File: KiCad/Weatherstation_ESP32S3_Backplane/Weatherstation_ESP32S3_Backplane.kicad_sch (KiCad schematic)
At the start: 50 parts, among them J1 01x02 JST XH, J10 01x04 Molex KK254, J11 01x02 JST XH, J12 01x04 Molex KK254, J13 01x22 Generic socket, J14 01x22 Generic socket, J15 01x04 Generic header, J16 01x02 JST XH, J17 01x04 Molex KK254, J18 01x02 JST XH, J19 01x06 Generic socket, J2 01x03 JST XH, J20 01x06 Generic socket, J3 01x03 JST XH, J4 01x07 Generic socket, J5 01x08 Generic socket, J6 01x08 Generic socket, J7 01x04 JST XH, J8 01x04 Molex KK254, J9 282834-2 Screw Terminal, Q1 RFP12N10L, U1 LM7805, U2 MAX6675ISA+T

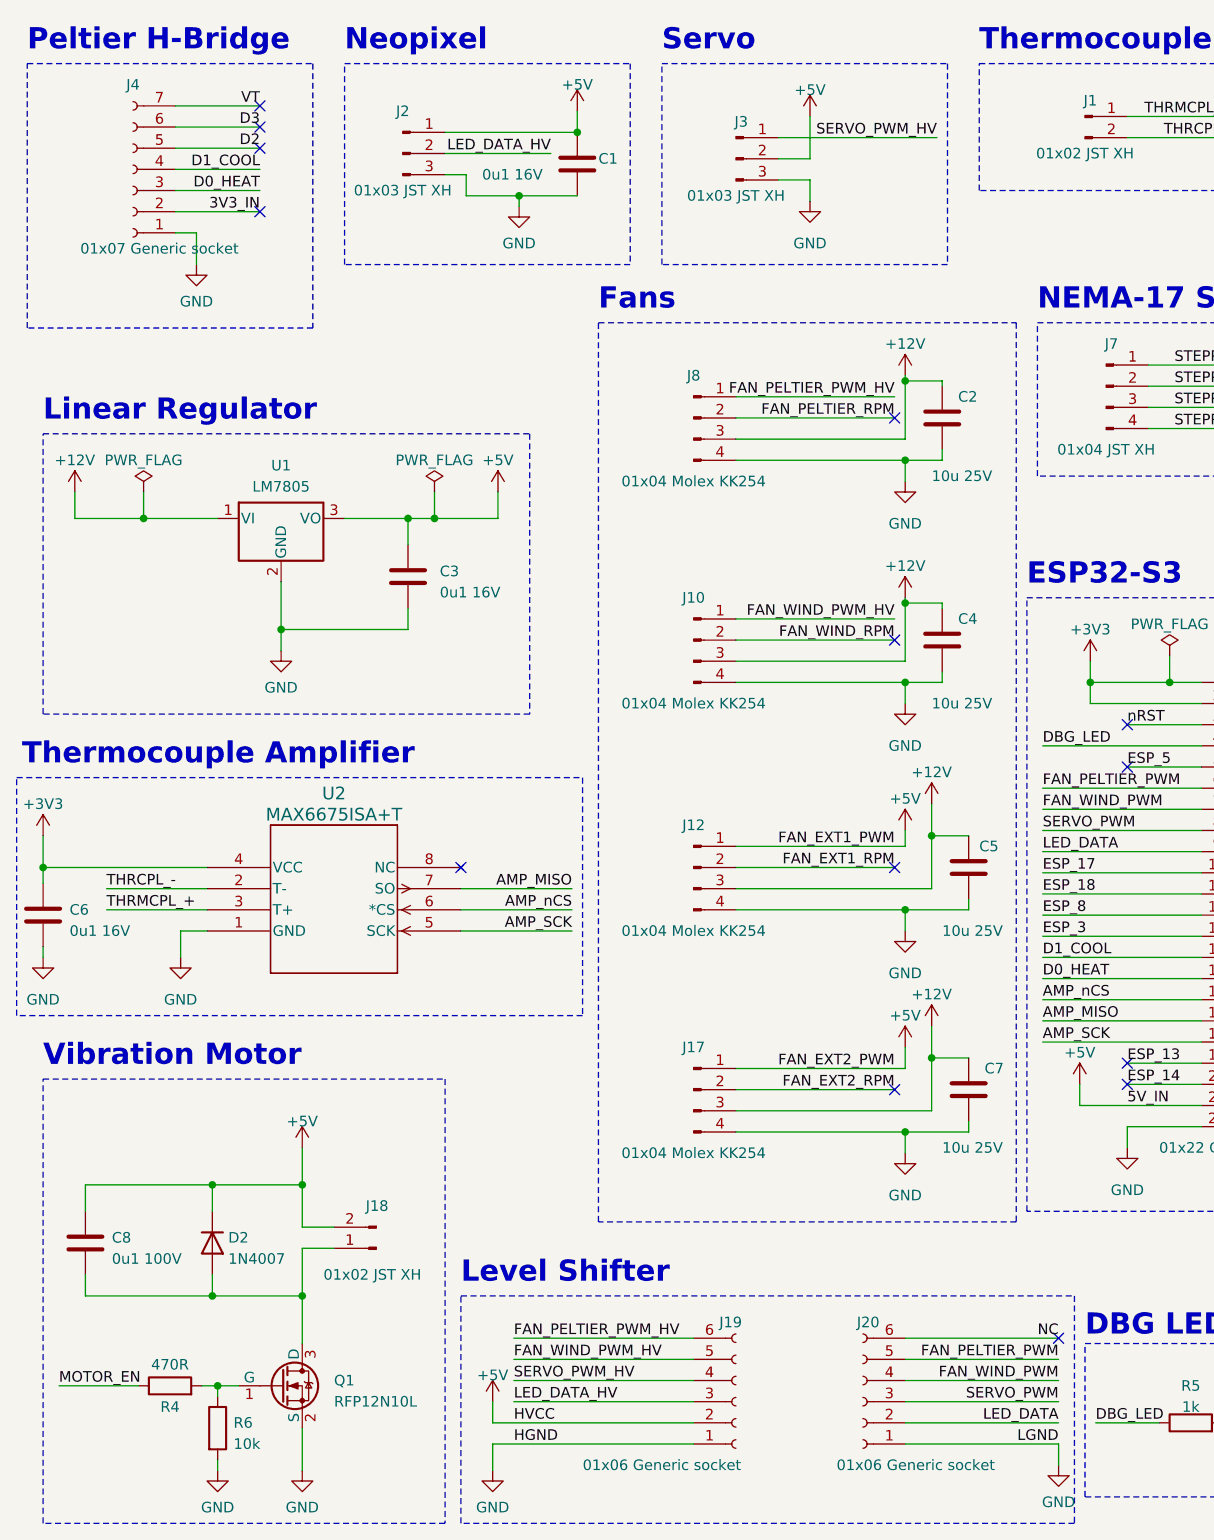
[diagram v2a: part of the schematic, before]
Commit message: Fixed known issues with PCB: Connected neopixel directly to ESP32, not through level shifter; Exchanged drain & source of vibration motor MOSFET; Added 0,33uF MLCC between pin 1 and gnd of LM7805;
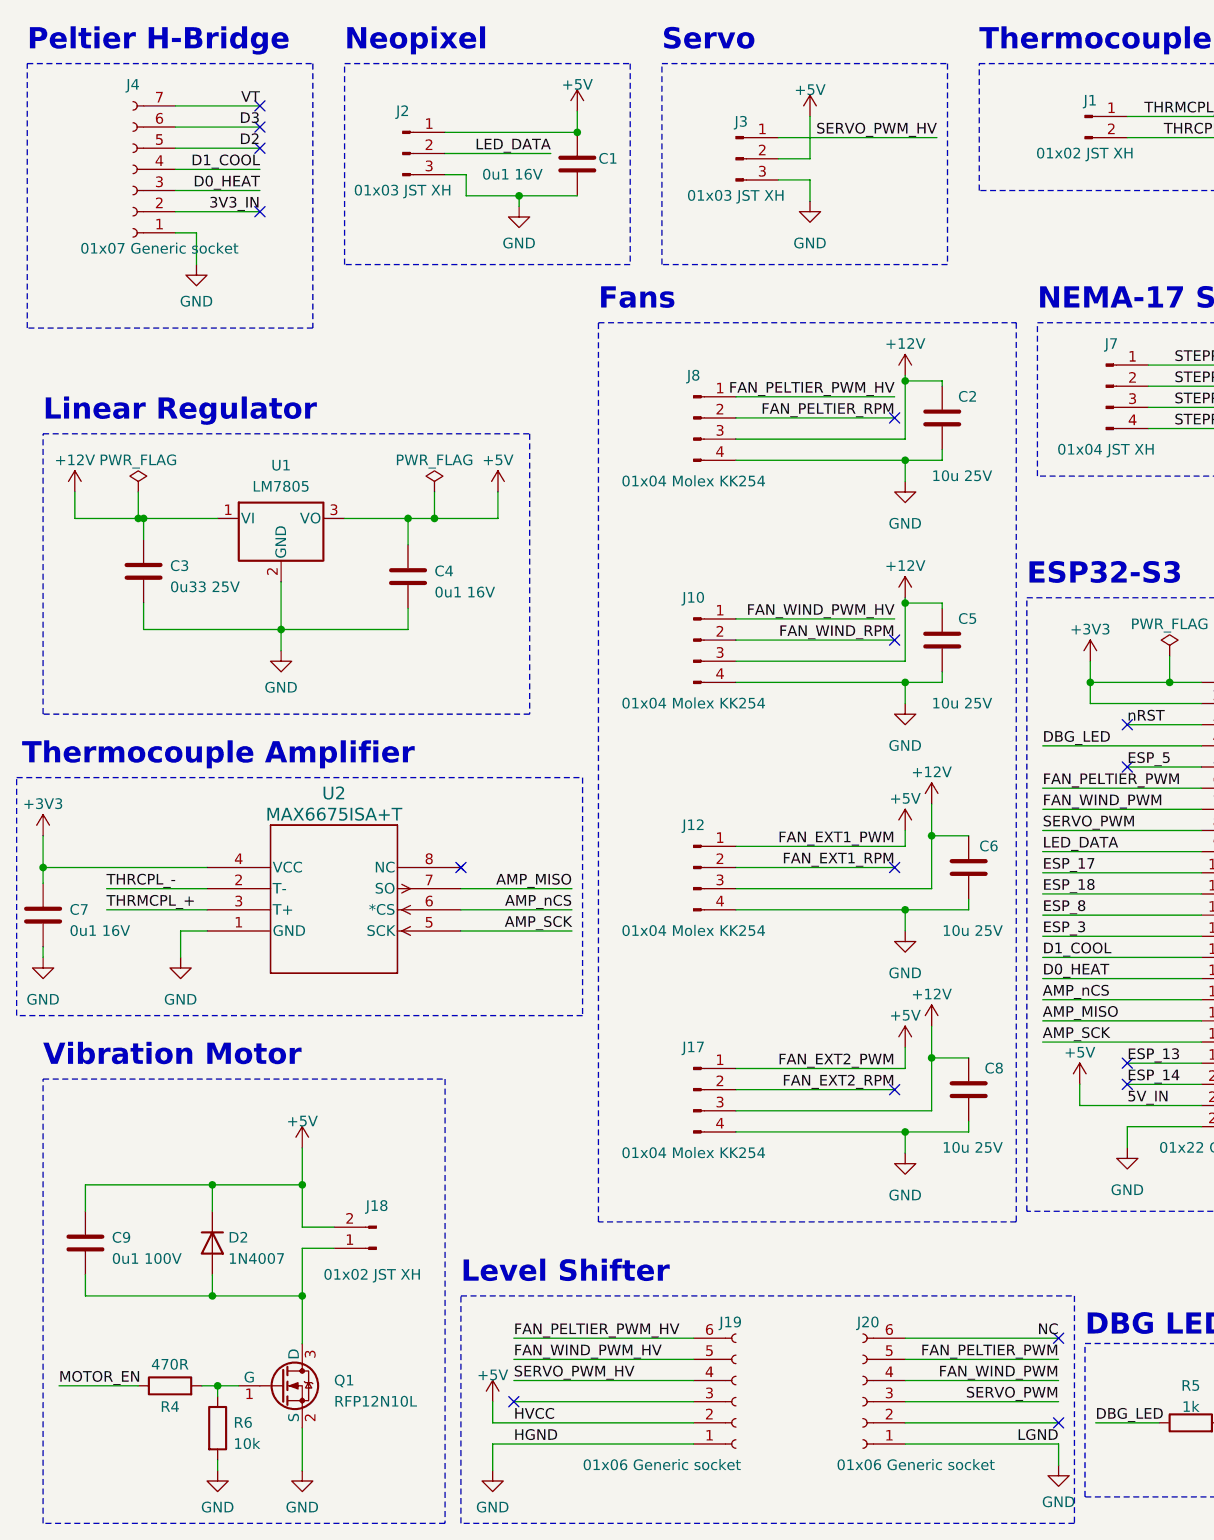
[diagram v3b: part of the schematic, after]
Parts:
- added C3: 0u33 25V, Capacitor_SMD:C_1206_3216Metric, symbol Device:C
- renumbered C3 to C4, C4 to C5, C5 to C6, C6 to C7, C7 to C8, C8 to C9
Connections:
- net +12V: now also C3.1
- net GND: now also C3.2
- net LED_DATA: now also J2.2 (Pin_2); no longer J20.2 (Pin_2)
- net LED_DATA_HV: no longer names the net of J19.3 (Pin_3)
- net LED_DATA_HV: no longer J2.2 (Pin_2)
- no-connect marks 29 -> 31
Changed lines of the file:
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@@
   (junction (at 120.65 147.32) (diameter 0) (color 0 0 0 0)
   )
+  (junction (at 28.575 73.66) (diameter 0) (color 0 0 0 0)
+  )
   (junction (at 120.65 120.65) (diameter 0) (color 0 0 0 0)
   )
@@
   )
   (no_connect (at 119.38 61.595))
+  (no_connect (at 139.065 182.245))
   (no_connect (at 203.2 95.885))
   (no_connect (at 119.38 88.265))
@@
   (no_connect (at 203.2 139.065))
   (no_connect (at 203.2 103.505))
+  (no_connect (at 73.66 179.705))
   (no_connect (at 43.18 36.83))
   (no_connect (at 43.18 29.21))
@@
     (stroke (width 0) (type default))
   )
-  (wire (pts (xy 20.955 73.66) (xy 29.21 73.66))
+  (wire (pts (xy 28.575 73.66) (xy 29.21 73.66))
+    (stroke (width 0) (type default))
+  )
+  (wire (pts (xy 20.955 73.66) (xy 28.575 73.66))
     (stroke (width 0) (type default))
   )
@@
     (stroke (width 0) (type default))
   )
+  (wire (pts (xy 45.72 86.995) (xy 29.21 86.995))
+    (stroke (width 0) (type default))
+  )
   (wire (pts (xy 123.825 111.76) (xy 128.27 111.76))
     (stroke (width 0) (type default))
@@
     (stroke (width 0) (type default))
   )
-  (wire (pts (xy 29.21 70.485) (xy 29.21 73.66))
-    (stroke (width 0) (type default))
-  )
   (wire (pts (xy 125.095 66.675) (xy 125.095 65.405))
     (stroke (width 0) (type default))
@@
     (stroke (width 0) (type default))
   )
+  (wire (pts (xy 29.21 73.66) (xy 29.21 76.2))
+    (stroke (width 0) (type default))
+  )
   (wire (pts (xy 128.27 147.32) (xy 128.27 146.05))
     (stroke (width 0) (type default))
@@
     (stroke (width 0) (type default))
   )
+  (wire (pts (xy 29.21 86.995) (xy 29.21 83.82))
+    (stroke (width 0) (type default))
+  )
   (wire (pts (xy 80.645 120.65) (xy 67.31 120.65))
     (stroke (width 0) (type default))
@@
     (stroke (width 0) (type default))
   )
+  (wire (pts (xy 28.575 70.485) (xy 28.575 73.66))
+    (stroke (width 0) (type default))
+  )
   (wire (pts (xy 120.65 147.32) (xy 120.65 149.86))
     (stroke (width 0) (type default))
@@
     (effects (font (size 1.27 1.27)) (justify right bottom))
   )
-  (label "LED_DATA_HV" (at 78.105 29.845 180) (fields_autoplaced)
+  (label "LED_DATA" (at 78.105 29.845 180) (fields_autoplaced)
     (effects (font (size 1.27 1.27)) (justify right bottom))
   )
@@
     (effects (font (size 1.27 1.27)) (justify right bottom))
   )
-  (label "LED_DATA" (at 139.065 182.245 180) (fields_autoplaced)
-    (effects (font (size 1.27 1.27)) (justify right bottom))
-  )
   (label "STEPPER_VM" (at 271.78 29.845 180) (fields_autoplaced)
     (effects (font (size 1.27 1.27)) (justify right bottom))
@@
     (effects (font (size 1.27 1.27)) (justify left bottom))
   )
-  (label "LED_DATA_HV" (at 73.66 179.705 0) (fields_autoplaced)
-    (effects (font (size 1.27 1.27)) (justify left bottom))
-  )
   (label "STEPPER_DIR" (at 213.36 47.625 0) (fields_autoplaced)
     (effects (font (size 1.27 1.27)) (justify left bottom))
@@
   (symbol (lib_id "Device:C") (at 128.27 115.57 0) (unit 1)
     (in_bom yes) (on_board yes) (dnp no)
-    (property "Reference" "C5" (at 129.54 113.03 0)
+    (property "Reference" "C6" (at 129.54 113.03 0)
       (effects (font (size 1.27 1.27)) (justify left))
     )
@@
       (project "Weatherstation_ESP32S3_Backplane"
         (path "/9f32fcd7-b7a2-400b-a555-9213e4bd23ed"
-          (reference "C5") (unit 1)
+          (reference "C6") (unit 1)
         )
       )
@@
     )
   )
+  (symbol (lib_id "Device:C") (at 29.21 80.01 0) (unit 1)
+    (in_bom yes) (on_board yes) (dnp no)
+    (property "Reference" "C3" (at 32.385 79.375 0)
+      (effects (font (size 1.27 1.27)) (justify left))
+    )
+    (property "Value" "0u33 25V" (at 32.385 81.915 0)
+      (effects (font (size 1.27 1.27)) (justify left))
+    )
+    (property "Footprint" "Capacitor_SMD:C_1206_3216Metric" (at 30.1752 83.82 0)
+      (effects (font (size 1.27 1.27)) hide)
+    )
+    (property "Datasheet" "~" (at 29.21 80.01 0)
+      (effects (font (size 1.27 1.27)) hide)
+    )
+    (property "LCSC Part #" "C1525" (at 29.21 80.01 0)
+      (effects (font (size 1.27 1.27)) hide)
+    )
+    (pin "1")
+    (pin "2")
+    (instances
+      (project "Weatherstation_ESP32S3_Backplane"
+        (path "/9f32fcd7-b7a2-400b-a555-9213e4bd23ed"
+          (reference "C3") (unit 1)
+        )
+      )
+    )
+  )
   (symbol (lib_id "Mechanical:MountingHole") (at 264.16 109.22 0) (unit 1)
     (in_bom yes) (on_board yes) (dnp no) (fields_autoplaced)
@@
   )
   (symbol (lib_id "Device:C") (at 60.96 80.645 0) (unit 1)
-    (in_bom yes) (on_board yes) (dnp no) (fields_autoplaced)
-    (property "Reference" "C3" (at 64.77 80.01 0)
+    (in_bom yes) (on_board yes) (dnp no)
+    (property "Reference" "C4" (at 64.135 80.01 0)
       (effects (font (size 1.27 1.27)) (justify left))
     )
-    (property "Value" "0u1 16V" (at 64.77 82.55 0)
+    (property "Value" "0u1 16V" (at 64.135 82.55 0)
       (effects (font (size 1.27 1.27)) (justify left))
     )
@@
       (project "Weatherstation_ESP32S3_Backplane"
         (path "/9f32fcd7-b7a2-400b-a555-9213e4bd23ed"
-          (reference "C3") (unit 1)
+          (reference "C4") (unit 1)
         )
       )
@@
   (symbol (lib_id "Device:C") (at 125.095 88.265 0) (unit 1)
     (in_bom yes) (on_board yes) (dnp no)
-    (property "Reference" "C4" (at 127 85.725 0)
+    (property "Reference" "C5" (at 127 85.725 0)
       (effects (font (size 1.27 1.27)) (justify left))
     )
@@
       (project "Weatherstation_ESP32S3_Backplane"
         (path "/9f32fcd7-b7a2-400b-a555-9213e4bd23ed"
-          (reference "C4") (unit 1)
+          (reference "C5") (unit 1)
         )
       )
@@
   (symbol (lib_id "Device:C") (at 17.145 121.285 180) (unit 1)
     (in_bom yes) (on_board yes) (dnp no) (fields_autoplaced)
-    (property "Reference" "C6" (at 20.32 120.65 0)
+    (property "Reference" "C7" (at 20.32 120.65 0)
       (effects (font (size 1.27 1.27)) (justify right))
     )
@@
       (project "Weatherstation_ESP32S3_Backplane"
         (path "/9f32fcd7-b7a2-400b-a555-9213e4bd23ed"
-          (reference "C6") (unit 1)
+          (reference "C7") (unit 1)
         )
       )
     )
   )
-  (symbol (lib_id "power:PWR_FLAG") (at 29.21 70.485 0) (unit 1)
+  (symbol (lib_id "power:PWR_FLAG") (at 28.575 70.485 0) (unit 1)
     (in_bom yes) (on_board yes) (dnp no)
-    (property "Reference" "#FLG01" (at 29.21 68.58 0)
+    (property "Reference" "#FLG01" (at 28.575 68.58 0)
       (effects (font (size 1.27 1.27)) hide)
     )
-    (property "Value" "PWR_FLAG" (at 29.21 66.675 0)
+    (property "Value" "PWR_FLAG" (at 28.575 66.675 0)
       (effects (font (size 1.27 1.27)))
     )
-    (property "Footprint" "" (at 29.21 70.485 0)
+    (property "Footprint" "" (at 28.575 70.485 0)
       (effects (font (size 1.27 1.27)) hide)
     )
-    (property "Datasheet" "~" (at 29.21 70.485 0)
+    (property "Datasheet" "~" (at 28.575 70.485 0)
       (effects (font (size 1.27 1.27)) hide)
     )
@@
   (symbol (lib_id "Device:C") (at 22.225 160.655 180) (unit 1)
     (in_bom yes) (on_board yes) (dnp no)
-    (property "Reference" "C8" (at 25.4 160.02 0)
+    (property "Reference" "C9" (at 25.4 160.02 0)
       (effects (font (size 1.27 1.27)) (justify right))
     )
@@
       (project "Weatherstation_ESP32S3_Backplane"
         (path "/9f32fcd7-b7a2-400b-a555-9213e4bd23ed"
-          (reference "C8") (unit 1)
+          (reference "C9") (unit 1)
         )
       )
@@
   (symbol (lib_id "Device:C") (at 128.27 142.24 0) (unit 1)
     (in_bom yes) (on_board yes) (dnp no)
-    (property "Reference" "C7" (at 130.175 139.7 0)
+    (property "Reference" "C8" (at 130.175 139.7 0)
       (effects (font (size 1.27 1.27)) (justify left))
     )
@@
       (project "Weatherstation_ESP32S3_Backplane"
         (path "/9f32fcd7-b7a2-400b-a555-9213e4bd23ed"
-          (reference "C7") (unit 1)
+          (reference "C8") (unit 1)
         )
       )
